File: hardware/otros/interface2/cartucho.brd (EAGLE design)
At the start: 39.4 x 23.8 mm, 6 parts, among them IC1 74AHC1G32DBV, IC2 SST39VF040N

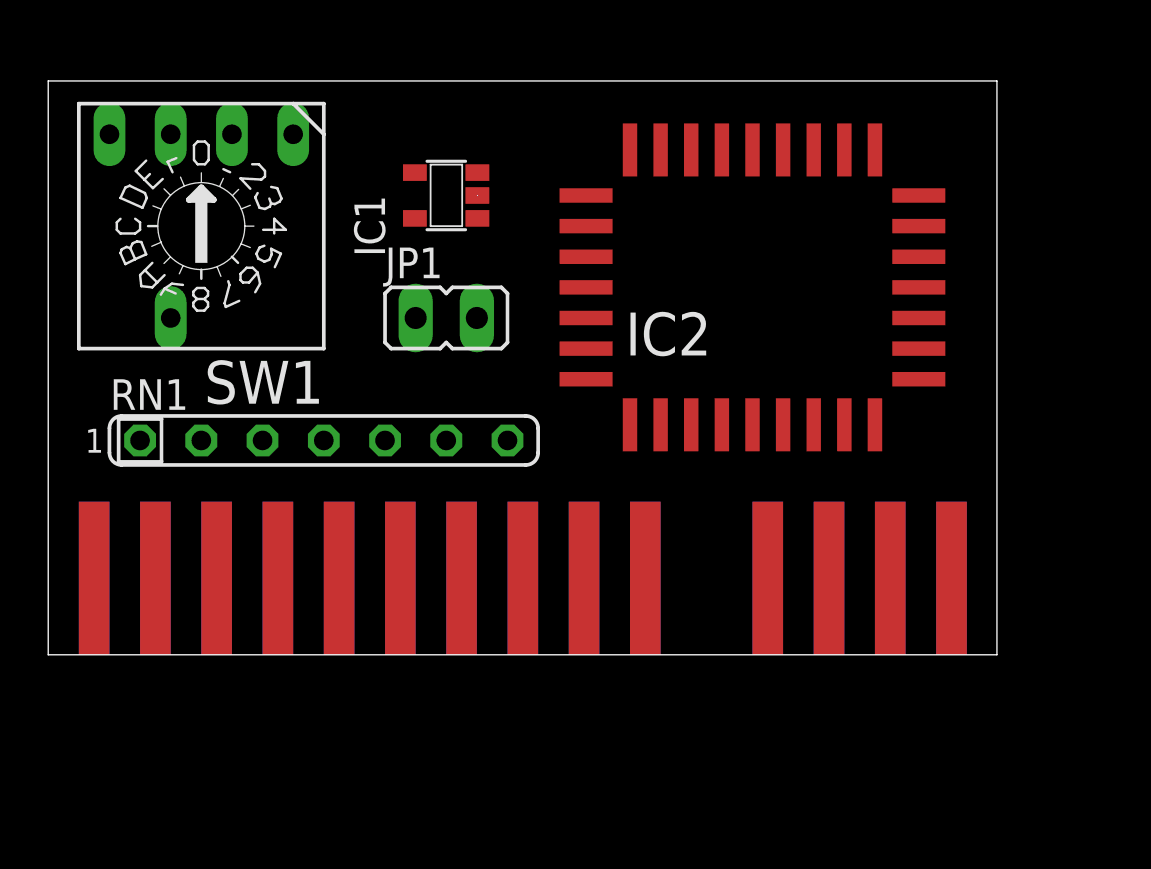
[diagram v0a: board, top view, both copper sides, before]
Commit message: 
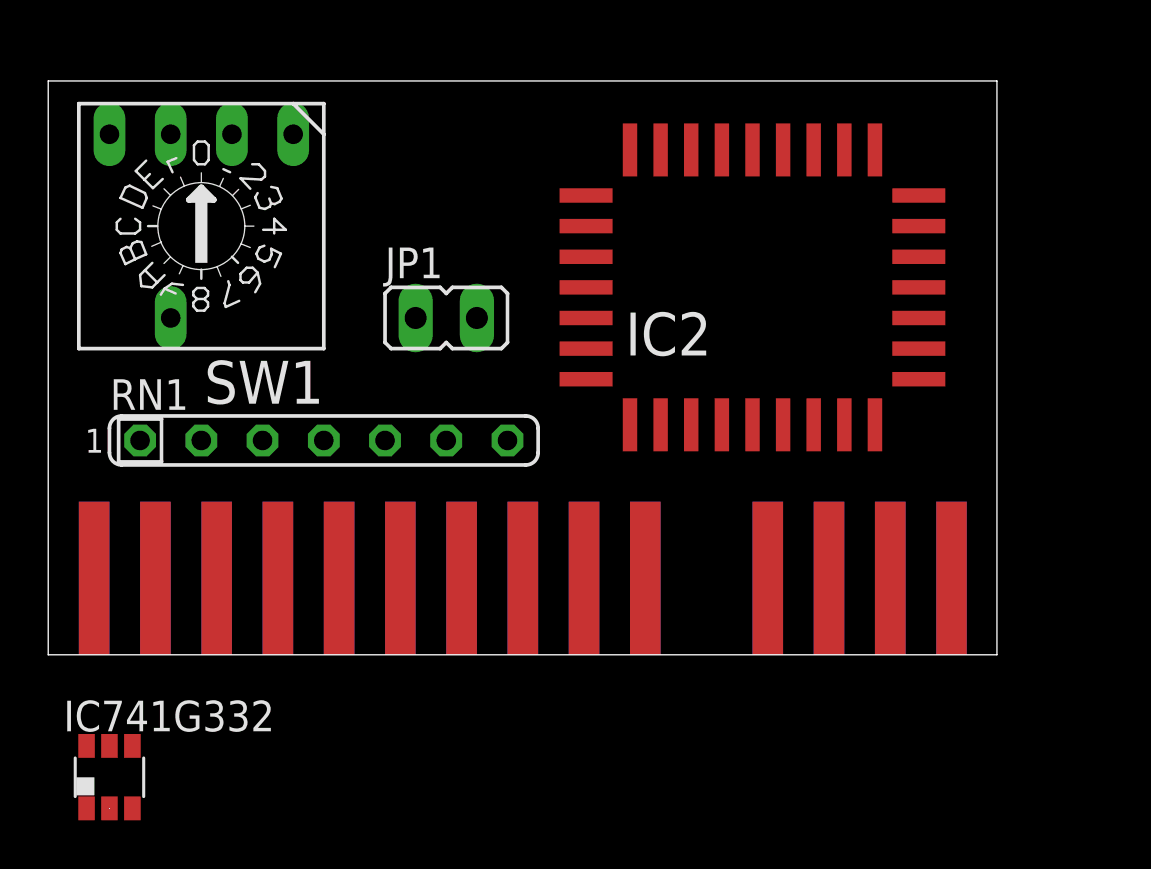
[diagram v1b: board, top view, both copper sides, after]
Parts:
- removed IC1: 74AHC1G32DBV, 74xx-little-us:SOT23-5
- added IC741G332: 741G3157DBVR, 74xx-little-de:DBV_R-PDSO-G6
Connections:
- new net RD: IC2.24
- net A14: now also IC741G332.3; no longer IC1.1
- net A15: now also IC741G332.1; no longer IC1.2
- net GND: now also IC741G332.2; no longer IC1.3
- net MREQ: now also IC741G332.6; no longer IC2.24
- net N$1: now also IC741G332.4; no longer IC1.4
- net VCC: now also IC741G332.5; no longer IC1.5
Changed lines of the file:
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@@
 </autorouter>
 <elements>
-<element name="IC1" library="74xx-little-us" package="SOT23-5" value="74AHC1G32DBV" x="16.51" y="19.05" rot="R90"/>
 <element name="IC2" library="memory" package="PLCC32R" value="SST39VF040N" x="29.21" y="15.24" rot="R90"/>
 <element name="U$1" library="SPECTRUM" package="BUS_CARTUCHO_IF2" value="IF2BUS" x="39.37" y="0"/>
@@
 <attribute name="OC_FARNELL" value="unknown" x="39.37" y="-30.48" size="1.778" layer="27" display="off"/>
 </element>
+<element name="IC741G332" library="74xx-little-de" package="DBV_R-PDSO-G6" value="741G3157DBVR" x="2.54" y="-5.08"/>
 </elements>
 <signals>
 <signal name="GND">
-<contactref element="IC1" pad="3"/>
 <contactref element="IC2" pad="16"/>
 <contactref element="SW1" pad="C"/>
 <contactref element="JP1" pad="1"/>
 <contactref element="U$1" pad="GND"/>
-<wire x1="17.8" y1="20" x2="36.11" y2="13.97" width="0" layer="19" extent="1-1"/>
-<wire x1="15.24" y1="13.97" x2="17.8" y2="20" width="0" layer="19" extent="1-1"/>
+<contactref element="IC741G332" pad="2"/>
+<wire x1="15.24" y1="13.97" x2="36.11" y2="13.97" width="0" layer="19" extent="1-1"/>
 <wire x1="5.08" y1="13.97" x2="15.24" y2="13.97" width="0" layer="19" extent="1-1"/>
 <wire x1="1.905" y1="3.175" x2="5.08" y2="13.97" width="0" layer="19" extent="16-16"/>
+<wire x1="2.54" y1="-6.37" x2="1.905" y2="3.175" width="0" layer="19" extent="1-16"/>
 </signal>
 <signal name="VCC">
-<contactref element="IC1" pad="5"/>
 <contactref element="IC2" pad="32"/>
 <contactref element="RN1" pad="1"/>
 <contactref element="U$1" pad="VCC"/>
 <contactref element="U$1" pad="ROMCS"/>
+<contactref element="IC741G332" pad="5"/>
 <wire x1="37.465" y1="3.175" x2="37.465" y2="3.175" width="0" layer="19" extent="1-16"/>
 <wire x1="22.31" y1="16.51" x2="37.465" y2="3.175" width="0" layer="19" extent="1-1"/>
-<wire x1="15.21" y1="18.1" x2="22.31" y2="16.51" width="0" layer="19" extent="1-1"/>
-<wire x1="3.81" y1="8.89" x2="15.21" y2="18.1" width="0" layer="19" extent="1-1"/>
+<wire x1="3.81" y1="8.89" x2="22.31" y2="16.51" width="0" layer="19" extent="1-1"/>
+<wire x1="2.54" y1="-3.78" x2="3.81" y2="8.89" width="0" layer="19" extent="1-1"/>
 </signal>
 <signal name="N$1">
-<contactref element="IC1" pad="4"/>
 <contactref element="IC2" pad="22"/>
-<wire x1="15.21" y1="20" x2="33.02" y2="20.94" width="0" layer="19" extent="1-1"/>
+<contactref element="IC741G332" pad="4"/>
+<wire x1="3.49" y1="-3.78" x2="33.02" y2="20.94" width="0" layer="19" extent="1-1"/>
 </signal>
 <signal name="A0">
@@
 </signal>
 <signal name="A14">
-<contactref element="IC1" pad="1"/>
 <contactref element="U$1" pad="A14"/>
-<wire x1="14.605" y1="3.175" x2="17.8" y2="18.1" width="0" layer="19" extent="1-1"/>
+<contactref element="IC741G332" pad="3"/>
+<wire x1="3.49" y1="-6.37" x2="14.605" y2="3.175" width="0" layer="19" extent="1-1"/>
 </signal>
 <signal name="A15">
-<contactref element="IC1" pad="2"/>
 <contactref element="U$1" pad="A15"/>
-<wire x1="17.8" y1="19.05" x2="34.925" y2="3.175" width="0" layer="19" extent="1-1"/>
+<contactref element="IC741G332" pad="1"/>
+<wire x1="1.59" y1="-6.37" x2="34.925" y2="3.175" width="0" layer="19" extent="1-1"/>
 </signal>
 <signal name="N$2">
@@
 <signal name="MREQ">
 <contactref element="U$1" pad="MREQ"/>
+<contactref element="IC741G332" pad="6"/>
+<wire x1="1.59" y1="-3.78" x2="19.685" y2="3.175" width="0" layer="19" extent="1-1"/>
+</signal>
+<signal name="RD">
 <contactref element="IC2" pad="24"/>
-<wire x1="19.685" y1="3.175" x2="30.48" y2="20.94" width="0" layer="19" extent="1-1"/>
+</signal>
+<signal name="WR">
 </signal>
 </signals>

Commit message: 
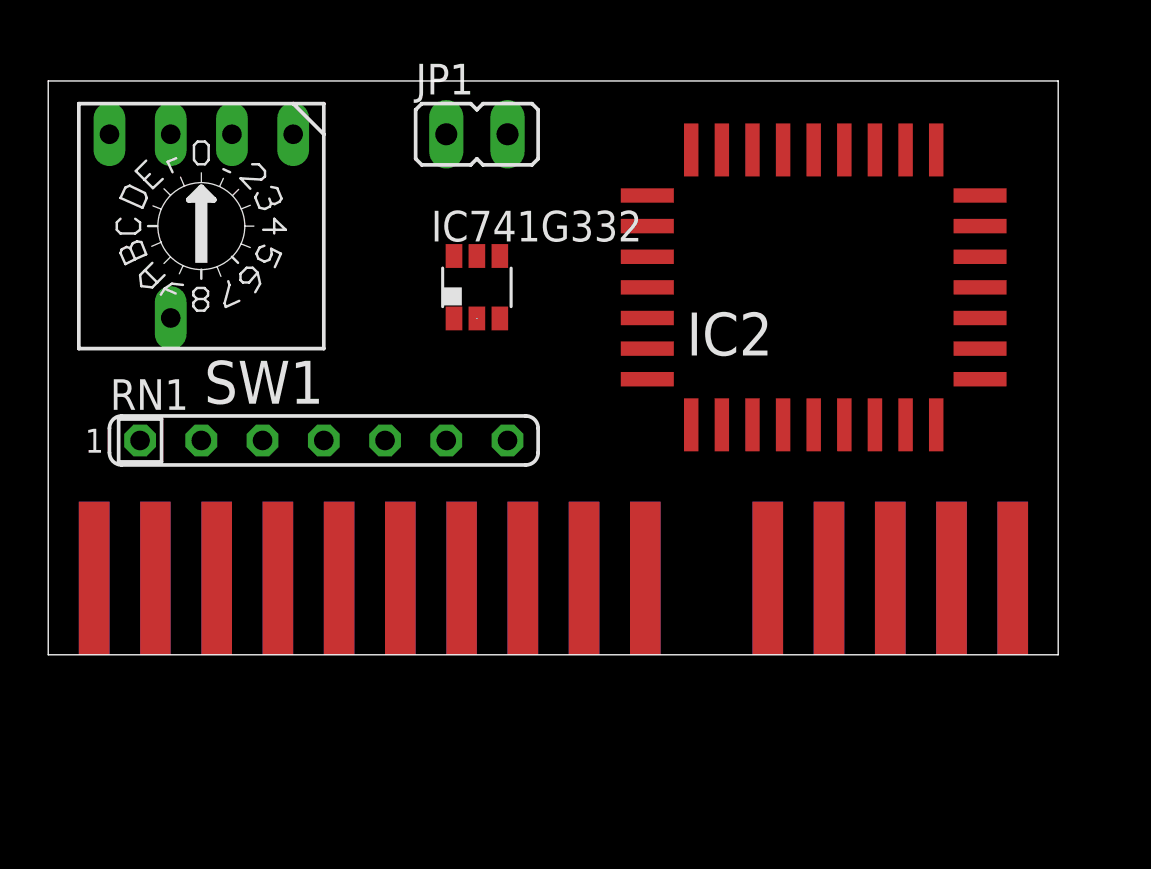
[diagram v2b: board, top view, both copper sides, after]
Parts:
- moved IC741G332 25.4 mm to (17.8, 15.2)
- moved JP1 7.73 mm to (17.8, 21.6)
- moved IC2 2.54 mm to (31.8, 15.2)
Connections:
- new net WR: U$1.WR
- net RD: now also U$1.RD
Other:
- board size 39.4 x 23.8 mm -> 41.9 x 23.8 mm

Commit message: 
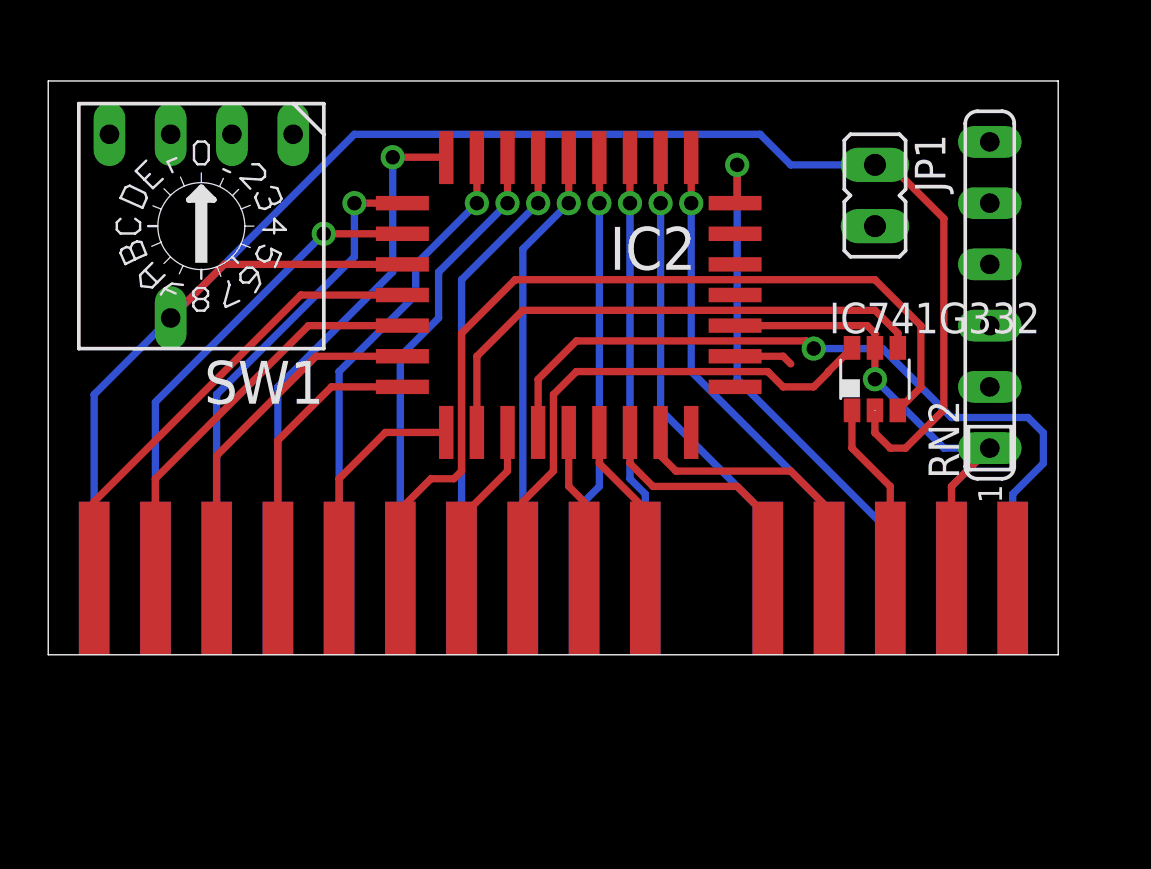
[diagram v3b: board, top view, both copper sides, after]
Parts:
- removed RN1: (no value), resistor-sil:SIL7
- added RN2: (no value), resistor-sil:SIL6
- moved IC741G332 16.9 mm to (34.3, 11.4)
- moved JP1 16.7 mm to (34.3, 19.1), turned to 180 degrees
- moved IC2 10.2 mm to (21.6, 14.9), turned to 270 degrees
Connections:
- net N$1 renamed CS
- net N$2: now also RN2.2; no longer RN1.3
- net N$3: now also RN2.3; no longer RN1.4
- net N$4: now also RN2.4; no longer RN1.5
- net N$5: now also RN2.5; no longer RN1.6
- net N$6: now also RN2.6; no longer RN1.7
- net VCC: now also RN2.1; no longer RN1.1
- net WR: now also IC2.31
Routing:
- net GND: track 0.00 -> 72.0 mm
- net A14: track 0.00 -> 36.4 mm
- net RD: track 0.00 -> 32.0 mm, vias 0 -> 1
- net VCC: track 0.00 -> 25.9 mm, vias 0 -> 1
- net CS: track 0.00 -> 22.4 mm
- net MREQ: track 0.00 -> 21.9 mm
- net D0: track 0.00 -> 21.7 mm, vias 0 -> 1
- net A12: track 0.00 -> 21.4 mm, vias 0 -> 1
- net D2: track 0.00 -> 20.4 mm, vias 0 -> 1
- net D1: track 0.00 -> 19.9 mm, vias 0 -> 1
- net A0: track 0.00 -> 19.8 mm, vias 0 -> 1
- net A7: track 0.00 -> 19.8 mm, vias 0 -> 1
- net D3: track 0.00 -> 19.5 mm
- net A6: track 0.00 -> 19.3 mm, vias 0 -> 1
- net A1: track 0.00 -> 19.3 mm, vias 0 -> 1
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
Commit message: 
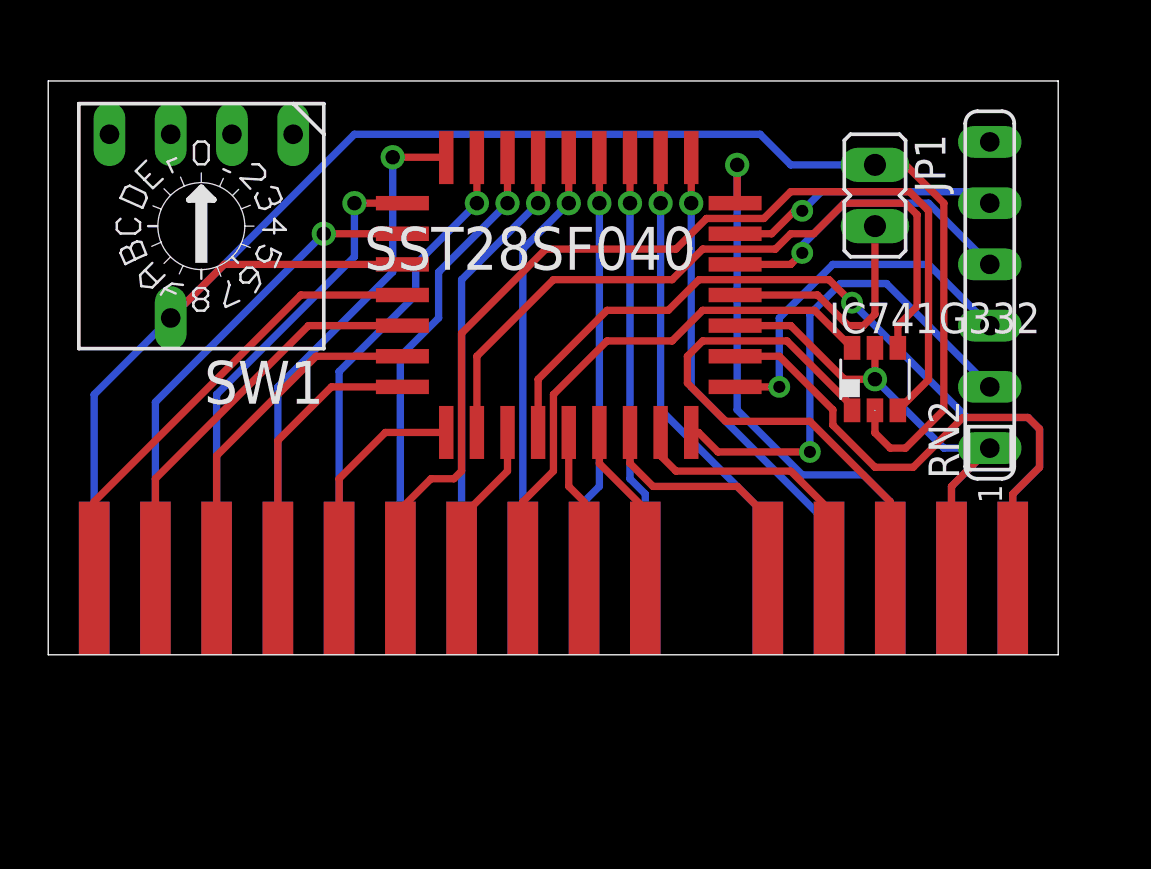
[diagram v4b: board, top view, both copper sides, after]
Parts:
- IC741G332: value 741G3157DBVR -> (none)
- SST28SF040: value SST39VF040N -> (none)
- renumbered IC2 to SST28SF040
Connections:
- net N$2: now also RN2.6; no longer RN2.2
- net N$6: now also RN2.2; no longer RN2.6
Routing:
- net N$6: track 0.00 -> 20.7 mm, vias 0 -> 1
- net WR: track 2.44 -> 22.6 mm
- net A15: track 7.62 -> 23.1 mm
- net N$3: track 0.00 -> 15.4 mm, vias 0 -> 1
- net N$4: track 0.00 -> 12.9 mm, vias 0 -> 1
- net N$5: track 0.00 -> 11.5 mm, vias 0 -> 1
- net N$2: track 0.00 -> 10.7 mm
- net CS: track 22.4 -> 30.1 mm
- net A14: track 36.4 -> 42.7 mm
- net RD: track 32.0 -> 33.9 mm
- net A12: track 21.4 -> 22.9 mm
- net MREQ: track 21.9 -> 22.6 mm

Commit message: 
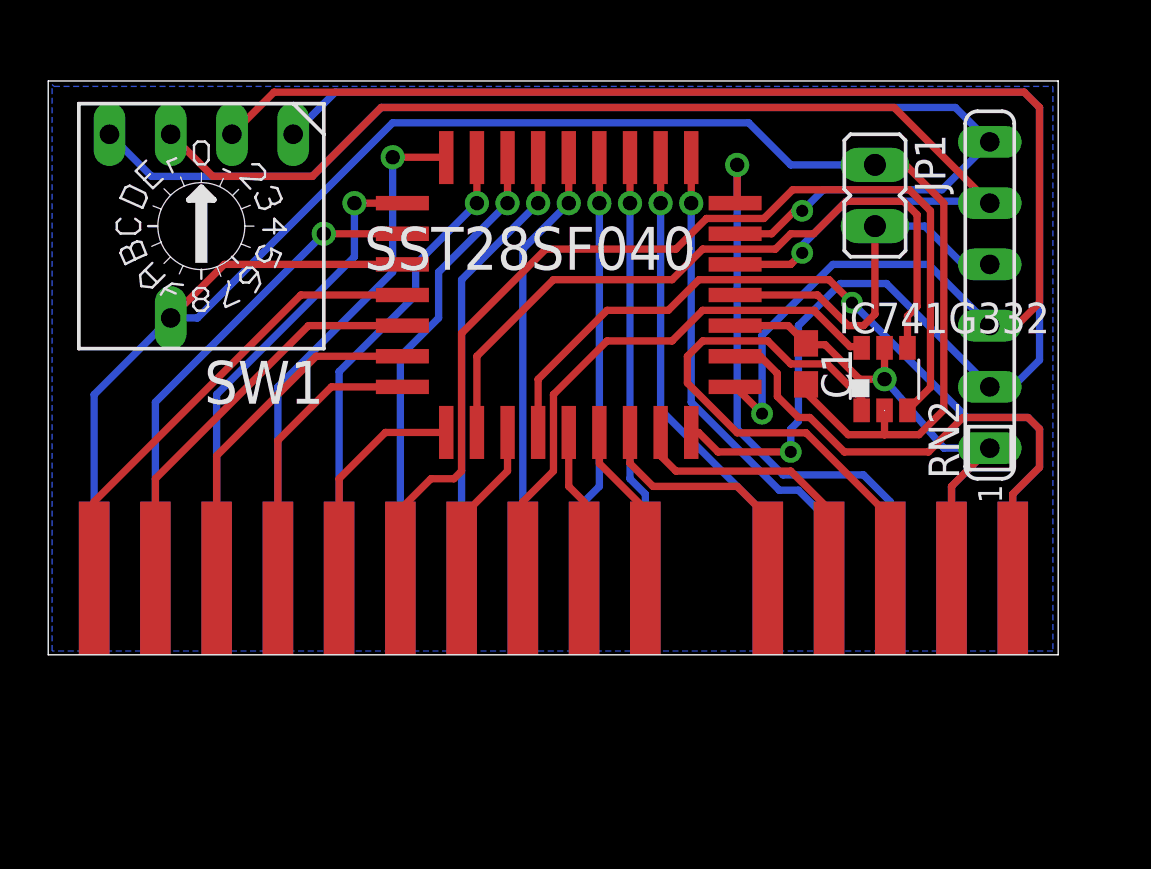
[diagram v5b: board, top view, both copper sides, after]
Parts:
- added C1: (no value), rcl:C0603
- moved IC741G332 0.40 mm to (34.7, 11.4)
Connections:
- net GND: now also C1.2
- net N$2: now also RN2.4; no longer RN2.6
- net N$3: now also SW1.2; no longer SW1.8
- net N$4: now also RN2.5; no longer RN2.4
- net N$5: now also RN2.6, SW1.8; no longer RN2.5, SW1.2
- net VCC: now also C1.1
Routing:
- net N$3: track 15.4 -> 61.7 mm
- net N$6: track 20.7 -> 65.2 mm
- net N$5: track 11.5 -> 51.2 mm
- net N$4: track 12.9 -> 49.4 mm
- net N$2: track 10.7 -> 16.1 mm
- net GND: track 72.3 -> 76.3 mm
- added copper zone on layer 16, net GND

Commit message: 
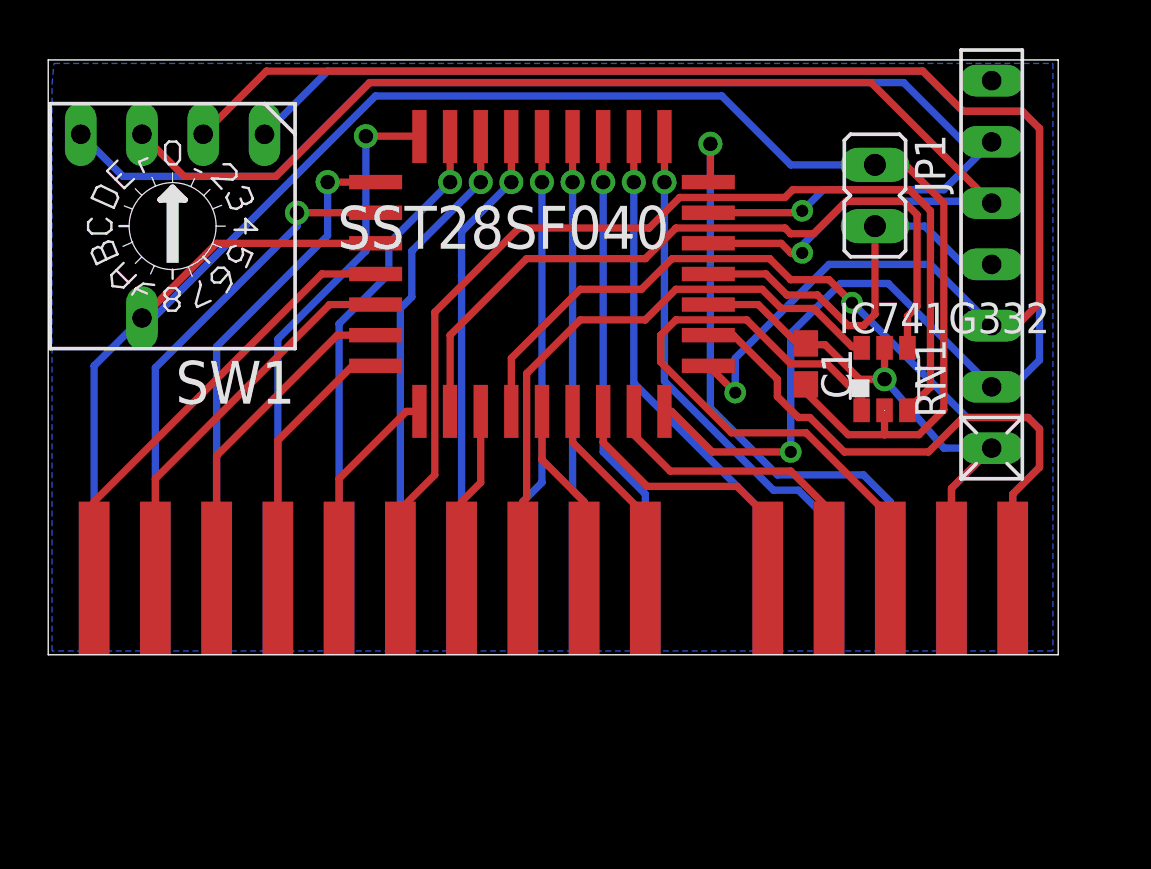
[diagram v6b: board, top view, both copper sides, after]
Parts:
- removed RN2: (no value), resistor-sil:SIL6
- added RN1: (no value), resistor-net:RN-7
- moved SST28SF040 1.41 mm to (20.5, 15.8)
- moved SW1 1.19 mm to (5.16, 17.8)
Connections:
- net N$2: now also RN1.4; no longer RN2.4
- net N$3: now also RN1.3; no longer RN2.3
- net N$4: now also RN1.5; no longer RN2.5
- net N$5: now also RN1.6; no longer RN2.6
- net N$6: now also RN1.2; no longer RN2.2
- net VCC: now also RN1.1; no longer RN2.1
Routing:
- net N$4: track 49.4 -> 52.7 mm
- net N$5: track 51.2 -> 54.4 mm
- net A15: track 23.5 -> 26.5 mm
- net N$6: track 65.2 -> 68.1 mm
- net GND: track 76.3 -> 78.3 mm
- net MREQ: track 23.0 -> 24.9 mm
- net VCC: track 26.2 -> 27.8 mm
- net N$2: track 16.1 -> 17.6 mm
- net RD: track 33.9 -> 35.4 mm
- net A7: track 20.3 -> 21.8 mm
- net A9: track 6.84 -> 8.31 mm
- net A8: track 10.5 -> 11.9 mm
- net A13: track 11.7 -> 13.2 mm
- net A12: track 23.4 -> 24.8 mm
- net A6: track 19.3 -> 20.6 mm
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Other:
- board size 41.9 x 23.8 mm -> 41.9 x 24.7 mm
